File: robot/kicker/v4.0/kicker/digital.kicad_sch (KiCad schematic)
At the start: 69 parts, among them J2 Conn_ARM_JTAG_SWD_10, J3 Conn_01x02, J4 Conn_01x04_Pin, Q5 BSS138K, SW2 BTN0, SW3 SW_DIP_x04, SW4 RST, U5 STM32F407VETx, U6 SK9822, U7 AT25DF041x-UxN-x, U8 SK9822, U9 AD8494, Y1 TAXM8M4RDBCCT2T, Y2 Q13FC13500005

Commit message: kicker power rework
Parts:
- removed C32: 4.7u 6.3V, Capacitor_SMD:C_0402_1005Metric, symbol Device:C
- removed C41, C46, C49: 100n 50V, Capacitor_SMD:C_0402_1005Metric, symbol Device:C
- removed C45, C47: 10n 50V, Capacitor_SMD:C_0402_1005Metric, symbol Device:C
- removed C50: 10u 6.3V, Capacitor_SMD:C_0402_1005Metric, symbol Device:C
- removed J3: Conn_01x02, Connector_JST:JST_SH_SM02B-SRSS-TB_1x02-1MP_P1.00mm_Horizontal, symbol Connector_Generic:Conn_01x02
- removed J4: Conn_01x04_Pin, Connector_PinHeader_2.54mm:PinHeader_1x04_P2.54mm_Vertical, symbol Connector:Conn_01x04_Pin
- removed L6: 650 @100MHz, Resistor_SMD:R_0603_1608Metric, symbol Device:L_Ferrite
- removed R62: 1M, Resistor_SMD:R_0402_1005Metric, symbol Device:R_US
- removed R63, R64: 10k, Resistor_SMD:R_0402_1005Metric, symbol Device:R_US
- removed U5: STM32F407VETx, Package_QFP:LQFP-100_14x14mm_P0.5mm, symbol MCU_ST_STM32F4:STM32F407VETx
- removed U9: AD8494, Package_SO:MSOP-8_3x3mm_P0.65mm, symbol Sensor_Temperature:AD8494
- added C6: 10n 50V, Capacitor_SMD:C_0402_1005Metric, symbol Device:C
- added C7: 1u 50V, Capacitor_SMD:C_0402_1005Metric, symbol Device:C
- added U2: STM32G474VETx, Package_QFP:LQFP-100_14x14mm_P0.5mm, symbol MCU_ST_STM32G4:STM32G474VETx
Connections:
- net +3V3: now also U2.100 (VDD), U2.24 (VDD), U2.49 (VDD), U2.6 (VBAT), U2.64 (VDD), U2.75 (VDD)
- net AUX_MISO: now also U2.80 (PC11)
- net AUX_MOSI: now also U2.81 (PC12)
- net AUX_NSS: now also U2.78 (PA15)
- net AUX_SCK: now also U2.79 (PC10)
- net BB_CENTER.AGPIO: now also U2.31 (PC5)
- net BB_CENTER.SCL: now also U2.47 (PB10)
- net BB_CENTER.SDA: now also U2.50 (PB11)
- net BB_LEFT.AGPIO: now also U2.21 (PA1)
- net BB_LEFT.INT: now also U2.67 (PC8)
- net BB_LEFT.RST: now also U2.66 (PC7)
- net BB_LEFT.SCL: now also U2.69 (PA8)
- net BB_LEFT.SDA: now also U2.68 (PC9)
- net BB_LEFT.~{DET}: now also U2.65 (PC6)
- net BB_RIGHT.AGPIO: now also U2.20 (PA0)
- net BB_RIGHT.INT: now also U2.92 (PB5)
- net BB_RIGHT.RST: now also U2.91 (PB4)
- net BB_RIGHT.SCL: now also U2.93 (PB6)
- net BB_RIGHT.SDA: now also U2.94 (PB7)
- net BB_RIGHT.~{DET}: now also U2.90 (PB3)
- net DBG_HDR1: now also U2.95 (PB8)
- net DBG_HDR2: now also U2.96 (PB9)
- net DOTSTAR_MOSI: now also U2.29 (PA7)
- net DOTSTAR_SCK: now also U2.27 (PA5)
- net FLASH_MISO: now also U2.53 (PB14)
- net FLASH_MOSI: now also U2.54 (PB15)
- net FLASH_NSS: now also U2.51 (PB12)
- net FLASH_SCK: now also U2.52 (PB13)
- net GND: now also C6.2, C7.2, U2.23 (VSS), U2.35 (VSSA), U2.48 (VSS), U2.63 (VSS), U2.74 (VSS), U2.99 (VSS)
- net MCU_BOOT_UART.RX: now also U2.71 (PA10)
- net MCU_BOOT_UART.TX: now also U2.70 (PA9)
- net SENSE_UART.RX: now also U2.25 (PA3)
- net SENSE_UART.TX: now also U2.22 (PA2)
- net SENSE_UART.~{DET}: now also U2.34 (PB2)
- net SWCLK: now also U2.77 (PA14)
- net SWDIO: now also U2.76 (PA13)
- net TEMP_PROBE: now also U2.30 (PC4)
- net USB_OTG_FS_D_N: now also U2.72 (PA11)
- net USB_OTG_FS_D_P: now also U2.73 (PA12)
- net USER_ADJ1: now also U2.32 (PB0)
- net USER_ADJ2: now also U2.33 (PB1)
- net V_{sense}_12v0: now also U2.16 (PC1)
- net V_{sense}_HV: now also U2.15 (PC0)
- net V_{sense}_V_{batt}: now also U2.28 (PA6)
- net +3V0: now reaches C37.1, C39.1
- net +3V0: now also C6.1, C7.1, U2.36 (VREF+), U2.37 (VDDA)
- net at C43.1, Y2.2: now also U2.8 (PC14)
- net at C42.1, Y2.1: now also U2.9 (PC15)
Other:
- note removed: "Temp Sensing"
- moved on the sheet: C37, C39

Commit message: sch passing ERC
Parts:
- removed C31, C33: 4.7u 6.3V, Capacitor_SMD:C_0402_1005Metric, symbol Device:C
- added C8: 100n 50V, Capacitor_SMD:C_0402_1005Metric, symbol Device:C
- added D2: XL-1608UWC-04, AT-LED:LED0603, symbol Device:LED
- added D4, D6: XL-1608UBC-04, AT-LED:LED0603, symbol Device:LED
- added Q1: BSS138K, Package_TO_SOT_SMD:SOT-23, symbol Device:Q_NMOS_GSD
- added R10, R25, R26, R9: 10k, Resistor_SMD:R_0402_1005Metric, symbol Device:R_Small_US
- added R11: 11.5k, Resistor_SMD:R_0402_1005Metric, symbol Device:R_Small_US
- added R12, R13, R14, R15, R29: 1k, Resistor_SMD:R_0402_1005Metric, symbol Device:R_Small_US
- added R16: 8k, Resistor_SMD:R_0402_1005Metric, symbol Device:R_Small_US
- added R17: 1.5k, Resistor_SMD:R_0402_1005Metric, symbol Device:R_Small_US
- added R18: 650, Resistor_SMD:R_0402_1005Metric, symbol Device:R_Small_US
- added R27, R28, R30: 0, Resistor_SMD:R_0402_1005Metric, symbol Device:R_Small_US
- added R3: 23.2k, Resistor_SMD:R_0402_1005Metric, symbol Device:R_Small_US
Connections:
- net AUX_MISO is gone; now on net BB_LEFT.~{DET}: U2.80 (PC11)
- net AUX_MOSI is gone; now on net BB_LEFT.INT: U2.81 (PC12)
- net AUX_NSS is gone; now on net BB_LEFT.SCL: U2.78 (PA15)
- net AUX_SCK is gone; now on net BB_LEFT.RST: U2.79 (PC10)
- net BB_LED1_BLUE is gone; now on net +3V3: R61.1
- net BB_LED2_BLUE is gone; now on net +3V3: R65.1
- net DBG_HDR1 is gone; now on net MCU_BOOT_UART.BOOT0: U2.95 (PB8)
- net DBG_HDR2 is gone; now on net LED_GREEN: U2.96 (PB9)
- net V_{sense}_12v0 is gone; now on net BB_CENTER.AGPIO: U2.16 (PC1)
- net +3V3: now also R10.1, R18.1, R9.1
- net +5V: now also R17.1
- net BB_CENTER.AGPIO: no longer U2.31 (PC5)
- net BB_CENTER.INT: now also U2.60 (PD13)
- net BB_CENTER.RST: now also U2.62 (PD15)
- net BB_CENTER.SCL: now also U2.67 (PC8); no longer U2.47 (PB10)
- net BB_CENTER.SDA: now also U2.68 (PC9); no longer U2.50 (PB11)
- net BB_CENTER.~{DET}: now also U2.61 (PD14)
- net BB_LEFT.AGPIO: now also U2.15 (PC0); no longer U2.21 (PA1)
- net BB_LEFT.INT: no longer U2.67 (PC8)
- net BB_LEFT.RST: no longer U2.66 (PC7)
- net BB_LEFT.SCL: no longer U2.69 (PA8)
- net BB_LEFT.SDA: now also U2.94 (PB7); no longer U2.68 (PC9)
- net BB_LEFT.~{DET}: no longer U2.65 (PC6)
- net BB_RIGHT.AGPIO: now also U2.17 (PC2); no longer U2.20 (PA0)
- net BB_RIGHT.INT: now also U2.57 (PD10); no longer U2.92 (PB5)
- net BB_RIGHT.RST: now also U2.59 (PD12); no longer U2.91 (PB4)
- net BB_RIGHT.SCL: now also U2.65 (PC6); no longer U2.93 (PB6)
- net BB_RIGHT.SDA: now also U2.66 (PC7); no longer U2.94 (PB7)
- net BB_RIGHT.~{DET}: now also U2.58 (PD11); no longer U2.90 (PB3)
- net CMD_{CHG}: now also U2.55 (PD8)
- net CMD_{CHIP}: now also U2.52 (PB13)
- net CMD_{KICK}: now also U2.53 (PB14)
- net DIP0: now also U2.82 (PD0)
- net DIP1: now also U2.83 (PD1)
- net DIP2: now also U2.84 (PD2)
- net DIP3: now also U2.85 (PD3)
- net DOTSTAR_MOSI: now also U2.5 (PE6); no longer U2.29 (PA7)
- net DOTSTAR_SCK: now also U2.1 (PE2); no longer U2.27 (PA5)
- net DRIB_UART.BOOT0: now also U2.44 (PE13)
- net DRIB_UART.RST: now also U2.45 (PE14)
- net DRIB_UART.RX: now also U2.46 (PE15)
- net DRIB_UART.TX: now also U2.47 (PB10)
- net DRIB_UART.~{DET}: now also U2.43 (PE12)
- net FLASH_MISO: now also U2.28 (PA6); no longer U2.53 (PB14)
- net FLASH_MOSI: now also U2.29 (PA7); no longer U2.54 (PB15)
- net FLASH_NSS: now also U2.26 (PA4); no longer U2.51 (PB12)
- net FLASH_SCK: now also U2.27 (PA5); no longer U2.52 (PB13)
- net GND: now also C8.2, D2.1 (K), Q1.2 (S), R12.2, R13.2, R14.2, R15.2, R26.2; no longer D10.1 (K), D11.1 (K)
- net LED_RED: now also U2.97 (PE0)
- net NRST: now also U2.14 (PG10)
- net SENSE_UART.BOOT0: now also U2.89 (PD7)
- net SENSE_UART.RST: now also U2.86 (PD4)
- net SENSE_UART.RX: now also U2.88 (PD6); no longer U2.25 (PA3)
- net SENSE_UART.TX: now also U2.87 (PD5); no longer U2.22 (PA2)
- net SENSE_UART.~{DET}: now also U2.90 (PB3); no longer U2.34 (PB2)
- net SWCLK: now also D9.3 (K2)
- net SWDIO: now also D9.4 (K3)
- net ShutdownInitiated: now also U2.93 (PB6)
- net USER_ADJ1: now also U2.39 (PE8); no longer U2.32 (PB0)
- net USER_ADJ2: now also U2.40 (PE9); no longer U2.33 (PB1)
- net USR_BTN: now also U2.92 (PB5)
- net V_{sense}_HV: now also R27.1, R28.1; no longer U2.15 (PC0)
- net V_{sense}_V_{batt}: now also U2.20 (PA0), R11.2, R12.1; no longer U2.28 (PA6)
- net RCC_OSC_P: now reaches C28.1, Y1.3
- net RCC_OSC_P: now also U2.12 (PF0)
- net RCC_OSC_N: now reaches U2.13 (PF1)
- net RCC_OSC_N: now also C27.1, Y1.1
- net V_{sense}_HV_FILT: now reaches U2.18 (PC3)
- net V_{sense}_HV_FILT: now also C8.1, R29.2
- net VSW_EN: now reaches U2.41 (PE10)
- net VSW_PGOOD: now reaches U2.42 (PE11)
- net RCC_OSC32_P: now reaches C43.1, U2.8 (PC14), Y2.2
- net RCC_OSC32_N: now reaches C42.1, U2.9 (PC15), Y2.1
- net LED_BB_BLUE: now reaches U2.98 (PE1)
- net LED_BB_BLUE: now also Q1.1 (G)
- net TEMP_PROBE: no longer names the net of U2.30 (PC4)
- net USB_OTG_FS_D_N: no longer names the net of U2.72 (PA11)
- net USB_OTG_FS_D_N: no longer D9.4 (K3)
- net USB_OTG_FS_D_P: no longer names the net of U2.73 (PA12)
- net USB_OTG_FS_D_P: no longer D9.3 (K2)
- new net: D4.2 (A), R9.2
- new net: D2.2 (A), R3.2
- new net: D6.2 (A), R10.2
- new net +BATT: R11.1, R3.1
- new net +VSW: R16.1
- new net BB_LED_DRAIN: D10.1 (K), D11.1 (K), D4.1 (K), D6.1 (K), Q1.3 (D)
- new net OPAMP3_VIN+: R27.2, U2.32 (PB0)
- new net OPAMP3_VIN-: R25.1, R26.1, U2.34 (PB2)
- new net OPAMP3_VOUT: R25.2, R30.1, U2.33 (PB1)
- new net V_{sense}_3v3: R15.1, R18.2, U2.25 (PA3)
- new net V_{sense}_5V0: R14.1, R17.2, U2.22 (PA2)
- new net V_{sense}_HV_PREFILT: R28.2, R29.1, R30.2
- new net V_{sense}_VSW: R13.1, R16.2, U2.21 (PA1)
- no-connect marks 14 -> 22
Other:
- note added: "-3dB cutoff 1.6kHz"
- note added: "Clocks"
- note added: "G=2"
- note added: "I_{out}@200V= 68uA I_{out}@20V = 6.8uA I_{out}@2V = 0.68uA"
- note added: "OPAMP3"
- note added: "V_{sense}_HV_AMPED"
- note added: "V_{sense}_HV_FB"
- note added: "V_{solenoid} Voltage Measurement"
- note added: "Voltage Monitoring"
- note removed: "Atl. Cfg. : TIM9 CH1 PWM Out"
- note removed: "Atl. Cfg. : TIM9 CH2 PWM Out"
- moved on the sheet: C27, C28, C34, C35, C36, C37, C38, C39, C40, C42, C43, C48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

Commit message: initial board structure from dxf
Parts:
- renumbered C44 to C10, C26 to C11, C48 to C12, C42 to C13, C43 to C14, C27 to C15, C28 to C16, C8 to C17, C29 to C18, C30 to C19, C34 to C20, C35 to C21, C36 to C22, C38 to C23, C40 to C24, C37 to C8, C39 to C9, D4 to D10, D6 to D11, D9 to D12, D12 to D4, D13 to D5, D2 to D6, D14 to D7, D10 to D8, D11 to D9, J2 to J4, Q5 to Q2, R66 to R10, R67 to R11, R3 to R12, R68 to R13, R61 to R14, R65 to R15, R9 to R16, R10 to R17, R59 to R18, R56 to R19, R47 to R20, R48 to R21, R49 to R22, R50 to R23, R51 to R24, R52 to R25, R53 to R26, R54 to R27, R55 to R28, R28 to R29, R27 to R30, R30 to R31, R29 to R32, R26 to R33, R25 to R34, R11 to R35, R16 to R36, R17 to R37, R18 to R38, R58 to R39, R12 to R40, R13 to R41, R14 to R42, R15 to R43, R57 to R44, SW2 to SW1, SW3 to SW2, SW4 to SW3, U6 to U3, U8 to U4, U2 to U5, U7 to U6, Y2 to Y1, Y1 to Y2

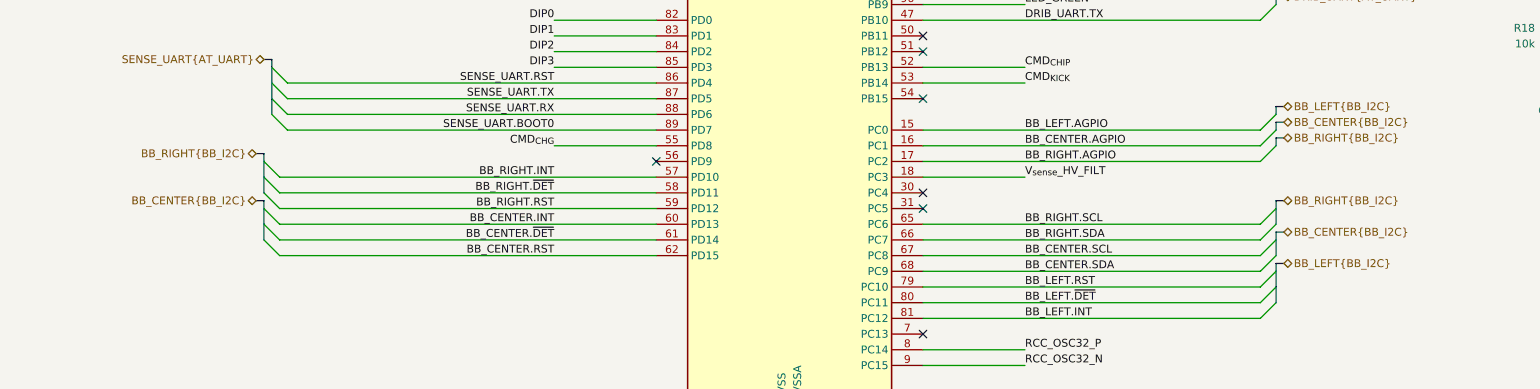
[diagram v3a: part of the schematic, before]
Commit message: update fusing and remove diode on 3v0 supply
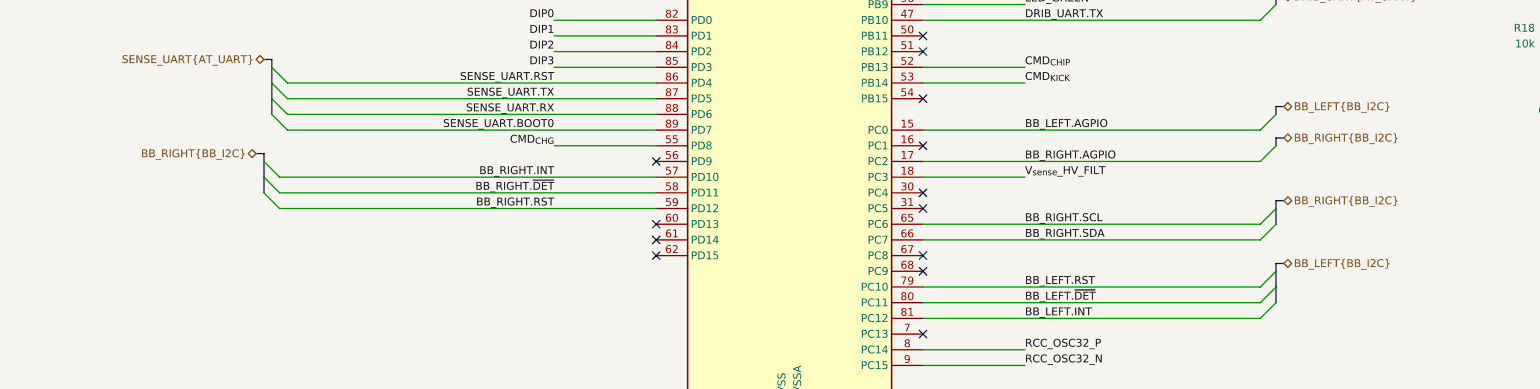
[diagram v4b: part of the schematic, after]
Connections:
- net BB_CENTER.AGPIO: no longer names the net of U5.16 (PC1)
- net BB_CENTER.INT: no longer names the net of U5.60 (PD13)
- net BB_CENTER.RST: no longer names the net of U5.62 (PD15)
- net BB_CENTER.SCL: no longer names the net of U5.67 (PC8)
- net BB_CENTER.SDA: no longer names the net of U5.68 (PC9)
- net BB_CENTER.~{DET}: no longer names the net of U5.61 (PD14)
- no-connect marks 22 -> 28

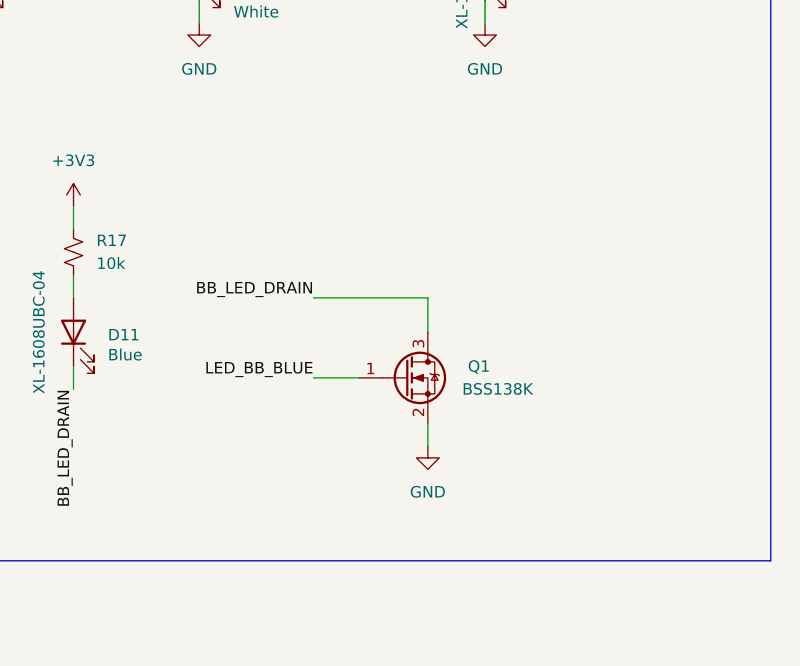
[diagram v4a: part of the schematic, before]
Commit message: coarse kicker placement done
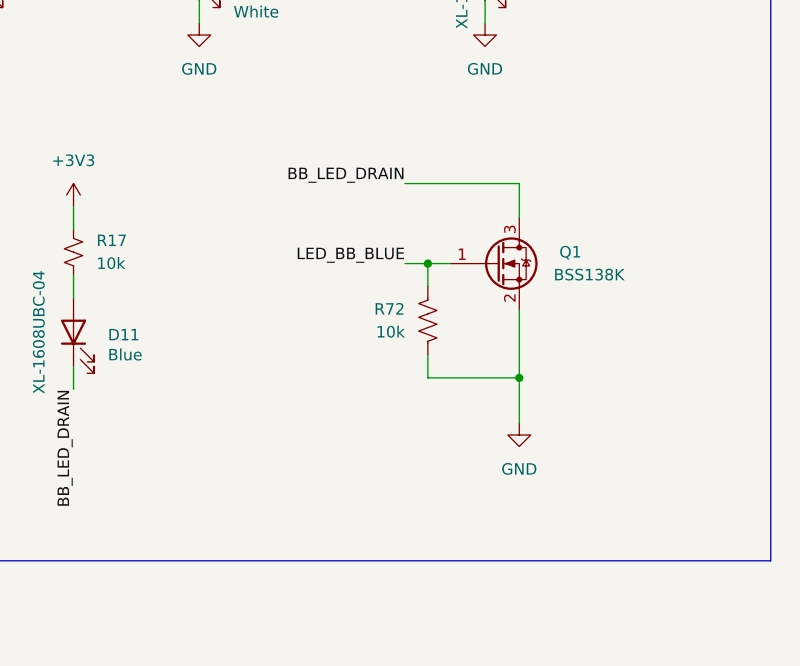
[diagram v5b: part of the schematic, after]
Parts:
- added R72: 10k, Resistor_SMD:R_0402_1005Metric, symbol Device:R_US
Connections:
- net GND: now also R72.1
- net LED_BB_BLUE: now also R72.2
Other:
- moved on the sheet: Q1
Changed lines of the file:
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@@
 	)
 	(junction
+		(at 533.4 119.38)
+		(diameter 0)
+		(color 0 0 0 0)
+	)
+	(junction
 		(at 240.03 71.12)
 		(diameter 0)
@@
 	)
 	(junction
+		(at 543.56 132.08)
+		(diameter 0)
+		(color 0 0 0 0)
+	)
+	(junction
 		(at 137.16 363.22)
 		(diameter 0)
@@
 	(wire
 		(pts
+			(xy 533.4 119.38) (xy 535.94 119.38)
+		)
+		(stroke
+			(width 0)
+			(type default)
+		)
+	)
+	(wire
+		(pts
 			(xy 38.1 238.76) (xy 50.8 238.76)
 		)
@@
 	(wire
 		(pts
+			(xy 533.4 132.08) (xy 543.56 132.08)
+		)
+		(stroke
+			(width 0)
+			(type default)
+		)
+	)
+	(wire
+		(pts
 			(xy 469.9 365.76) (xy 469.9 368.3)
 		)
@@
 	(wire
 		(pts
+			(xy 543.56 132.08) (xy 543.56 137.16)
+		)
+		(stroke
+			(width 0)
+			(type default)
+		)
+	)
+	(wire
+		(pts
 			(xy 262.89 147.32) (xy 279.4 147.32)
 		)
@@
 	(wire
 		(pts
-			(xy 533.4 123.19) (xy 533.4 127)
+			(xy 543.56 110.49) (xy 543.56 114.3)
 		)
 		(stroke
@@
 	(wire
 		(pts
-			(xy 533.4 137.16) (xy 533.4 139.7)
+			(xy 543.56 124.46) (xy 543.56 132.08)
 		)
 		(stroke
@@
 		)
 	)
+	(wire
+		(pts
+			(xy 533.4 129.54) (xy 533.4 132.08)
+		)
+		(stroke
+			(width 0)
+			(type default)
+		)
+	)
 	(polyline
 		(pts
@@
 	(wire
 		(pts
+			(xy 533.4 119.38) (xy 533.4 121.92)
+		)
+		(stroke
+			(width 0)
+			(type default)
+		)
+	)
+	(wire
+		(pts
 			(xy 494.03 262.89) (xy 494.03 267.97)
 		)
@@
 	(wire
 		(pts
-			(xy 520.7 123.19) (xy 533.4 123.19)
+			(xy 530.86 110.49) (xy 543.56 110.49)
 		)
 		(stroke
@@
 	(wire
 		(pts
-			(xy 520.7 132.08) (xy 525.78 132.08)
+			(xy 530.86 119.38) (xy 533.4 119.38)
 		)
 		(stroke
@@
 	)
 	(label "LED_BB_BLUE"
-		(at 520.7 132.08 180)
+		(at 530.86 119.38 180)
 		(fields_autoplaced yes)
 		(effects
@@
 	)
 	(label "BB_LED_DRAIN"
-		(at 520.7 123.19 180)
+		(at 530.86 110.49 180)
 		(fields_autoplaced yes)
 		(effects
@@
 	)
 	(symbol
+		(lib_id "Device:R_US")
+		(at 533.4 125.73 0)
+		(mirror x)
+		(unit 1)
+		(exclude_from_sim no)
+		(in_bom yes)
+		(on_board yes)
+		(dnp no)
+		(fields_autoplaced yes)
+		(property "Reference" "R72"
+			(at 530.86 124.46 0)
+			(effects
+				(font
+					(size 1.27 1.27)
+				)
+				(justify right)
+			)
+		)
+		(property "Value" "10k"
+			(at 530.86 127 0)
+			(effects
+				(font
+					(size 1.27 1.27)
+				)
+				(justify right)
+			)
+		)
+		(property "Footprint" "Resistor_SMD:R_0402_1005Metric"
+			(at 534.416 125.476 90)
+			(effects
+				(font
+					(size 1.27 1.27)
+				)
+				(hide yes)
+			)
+		)
+		(property "Datasheet" "~"
+			(at 533.4 125.73 0)
+			(effects
+				(font
+					(size 1.27 1.27)
+				)
+				(hide yes)
+			)
+		)
+		(property "Description" "Resistor, US symbol"
+			(at 533.4 125.73 0)
+			(effects
+				(font
+					(size 1.27 1.27)
+				)
+				(hide yes)
+			)
+		)
+		(pin "1"
+		)
+		(pin "2"
+		)
+		(instances
+			(project "kicker"
+				(path "/7c007fad-bfbf-4e78-a837-1f8089552516/18b5a777-2ae2-444a-8013-2f46c3974bf2"
+					(reference "R72")
+					(unit 1)
+				)
+			)
+		)
+	)
+	(symbol
 		(lib_id "power:+3V3")
 		(at 49.53 80.01 0)
@@
 	(symbol
 		(lib_id "power:GND")
-		(at 533.4 139.7 0)
+		(at 543.56 137.16 0)
 		(unit 1)
 		(exclude_from_sim no)
@@
 		(fields_autoplaced yes)
 		(property "Reference" "#PWR041"
-			(at 533.4 146.05 0)
+			(at 543.56 143.51 0)
 			(effects
 				(font
@@
 		)
 		(property "Value" "GND"
-			(at 533.4 144.78 0)
+			(at 543.56 142.24 0)
 			(effects
 				(font
@@
 		)
 		(property "Footprint" ""
-			(at 533.4 139.7 0)
+			(at 543.56 137.16 0)
 			(effects
 				(font
@@
 		)
 		(property "Datasheet" ""
-			(at 533.4 139.7 0)
+			(at 543.56 137.16 0)
 			(effects
 				(font
@@
 		)
 		(property "Description" "Power symbol creates a global label with name \"GND\" , ground"
-			(at 533.4 139.7 0)
+			(at 543.56 137.16 0)
 			(effects
 				(font
@@
 	(symbol
 		(lib_id "Device:Q_NMOS_GSD")
-		(at 530.86 132.08 0)
+		(at 541.02 119.38 0)
 		(unit 1)
 		(exclude_from_sim no)
@@
 		(dnp no)
 		(property "Reference" "Q1"
-			(at 537.845 130.81 0)
+			(at 548.005 118.11 0)
 			(effects
 				(font
@@
 		)
 		(property "Value" "BSS138K"
-			(at 537.21 133.3499 0)
+			(at 547.37 120.6499 0)
 			(effects
 				(font
@@
 		)
 		(property "Footprint" "Package_TO_SOT_SMD:SOT-23"
-			(at 535.94 129.54 0)
+			(at 546.1 116.84 0)
 			(effects
 				(font
@@
 		)
 		(property "Datasheet" "~"
-			(at 530.86 132.08 0)
+			(at 541.02 119.38 0)
 			(effects
 				(font
@@
 		)
 		(property "Description" "N-MOSFET transistor, gate/source/drain"
-			(at 530.86 132.08 0)
+			(at 541.02 119.38 0)
 			(effects
 				(font

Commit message: kicker passing DRC
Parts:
- J4: footprint AT-Connectors:Samtec-2x5pin-0.5mm -> AT-Connectors:Samtec-2x5pin-1.27mm
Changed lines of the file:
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@@
 			)
 		)
-		(property "Footprint" "AT-Connectors:Samtec-2x5pin-0.5mm"
+		(property "Footprint" "AT-Connectors:Samtec-2x5pin-1.27mm"
 			(at 49.53 99.06 0)
 			(effects

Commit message: Adjust for mechanical constraints and route board
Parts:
- removed D10, D11: XL-1608UBC-04, AT-LED:LED0603, symbol Device:LED
- removed R16, R17: 10k, Resistor_SMD:R_0402_1005Metric, symbol Device:R_Small_US
- RV1, RV2: footprint Potentiometer_SMD:Potentiometer_Bourns_3269X_Horizontal -> Potentiometer_SMD:Potentiometer_Bourns_3269P_Horizontal
- renumbered C20 to C10, C7 to C11, C21 to C12, C22 to C13, C23 to C14, C8 to C15, C24 to C16, C9 to C17, C17 to C18, C10 to C19, C13 to C20, C15 to C21, C14 to C22, C16 to C23, C12 to C24, C11 to C6, C18 to C7, C19 to C8, C6 to C9, D12 to D3, D8 to D4, D4 to D5, D9 to D6, D5 to D7, D6 to D8, D7 to D9, Q2 to Q1, Q1 to Q2, R20 to R11, R21 to R12, R22 to R13, R23 to R14, R24 to R15, R25 to R16, R26 to R17, R27 to R18, R28 to R19, R19 to R20, R44 to R21, R39 to R22, R29 to R23, R30 to R24, R33 to R25, R34 to R26, R18 to R27, R31 to R28, R32 to R29, R14 to R30, R10 to R31, R15 to R32, R35 to R33, R40 to R34, R11 to R35, R41 to R37, R12 to R38, R37 to R39, R42 to R40, R38 to R41, R43 to R42, R72 to R43, R13 to R44, U5 to U3, U3 to U4, U6 to U5, U4 to U6
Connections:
- net NRST: now also D3.1 (K1); no longer D3.6 (K5)
- net USR_BTN: now also D3.6 (K5); no longer D3.5 (K4)
- net V_{sense}_HV: now also D3.5 (K4); no longer D3.1 (K1)
